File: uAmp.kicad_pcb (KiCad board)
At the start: 2 copper layers, 45 x 24 mm, 18 parts, among them J1 PinHeader_1x07, U1 THAT1512P08-U

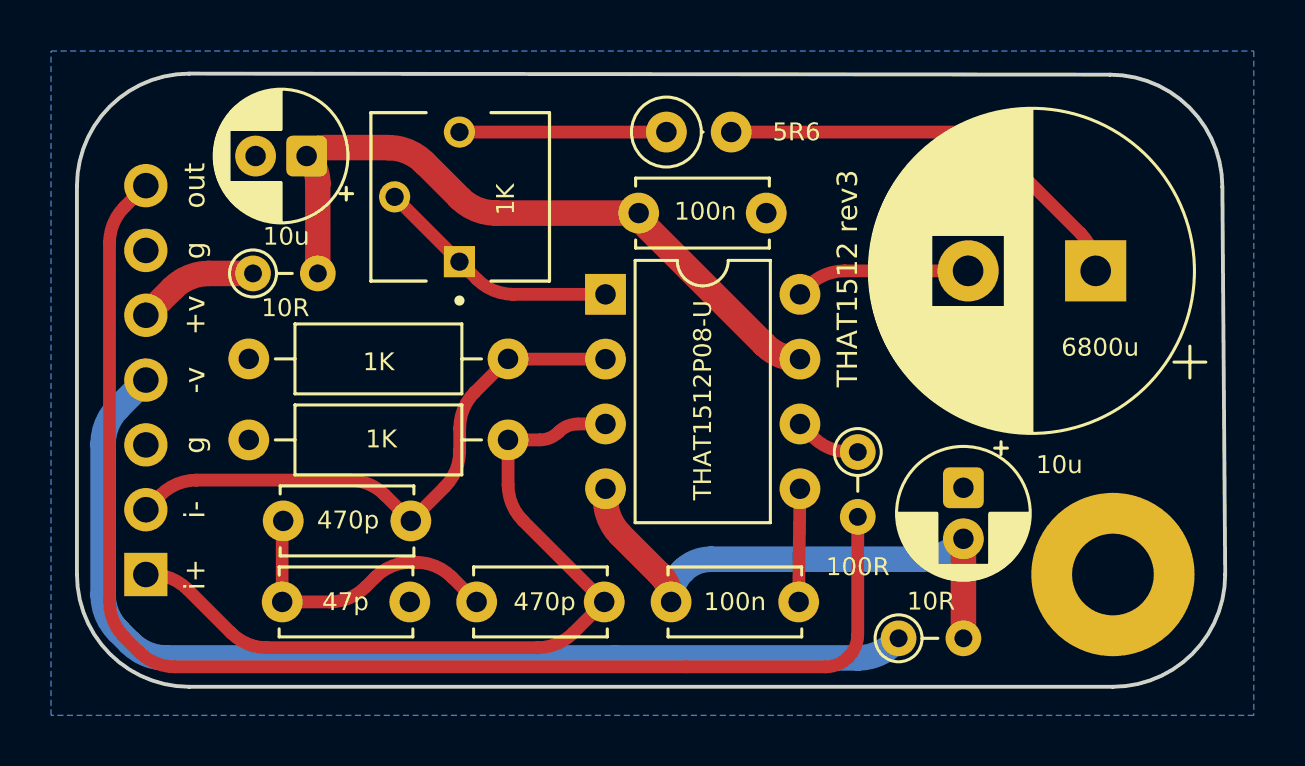
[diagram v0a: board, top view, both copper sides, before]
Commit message: Rename to uAmp; rev3 layout rework, C6 part number, rev2-style render
- Project renamed thatmicpre -> uAmp (files, README title, backups ignore).
- Layout (owner): U1, RV1, C5-C8, R1, R2, R4, R6 moved; GND pour now on
  both layers; header silk relabelled OUT/GND/+15V/-15V/GND/IN-/IN+;
  "uAmp" and "REV.3" added.
- Tidy after the moves: unfillet, collapse drag stubs, redraw seven
  jogged runs (U1 pins 2/3/4/6/7, R4-C7, C6 pad 1) as clean 45-degree
  paths, delete an accidental B.Cu duplicate of the +15V J1-R4 run, J1
  pad 6 solid to the pour, then re-fillet (one corner by RV1 at 0.8 mm
  to keep clearance). Placement, silk and pour untouched by the tidy.
  DRC with schematic parity: 0 errors, 0 unconnected, 0 parity.
- C6 = Nichicon UVZ0J682MHD (6800 uF 6.3 V, 12.5 x 25 mm, 5 mm pitch) in
  schematic, board and BOM; polarized is correct at zero bias, and no
  bipolar 6800 uF fits the footprint.
- README: SSM2019 substitution notes (owner).
- uAmp_rev3_render.png: the rev2 Blender scene (camera, tuned lights,
  world, shadow catcher) with the rev3 board swapped in and per-resistor
  colour bands, composited in Photoshop with the owner's backdrop and
  grade (the PSD is not in the repo). schematic.pdf regenerated.

Co-Authored-By: Claude Opus 5.5 <noreply@anthropic.com>
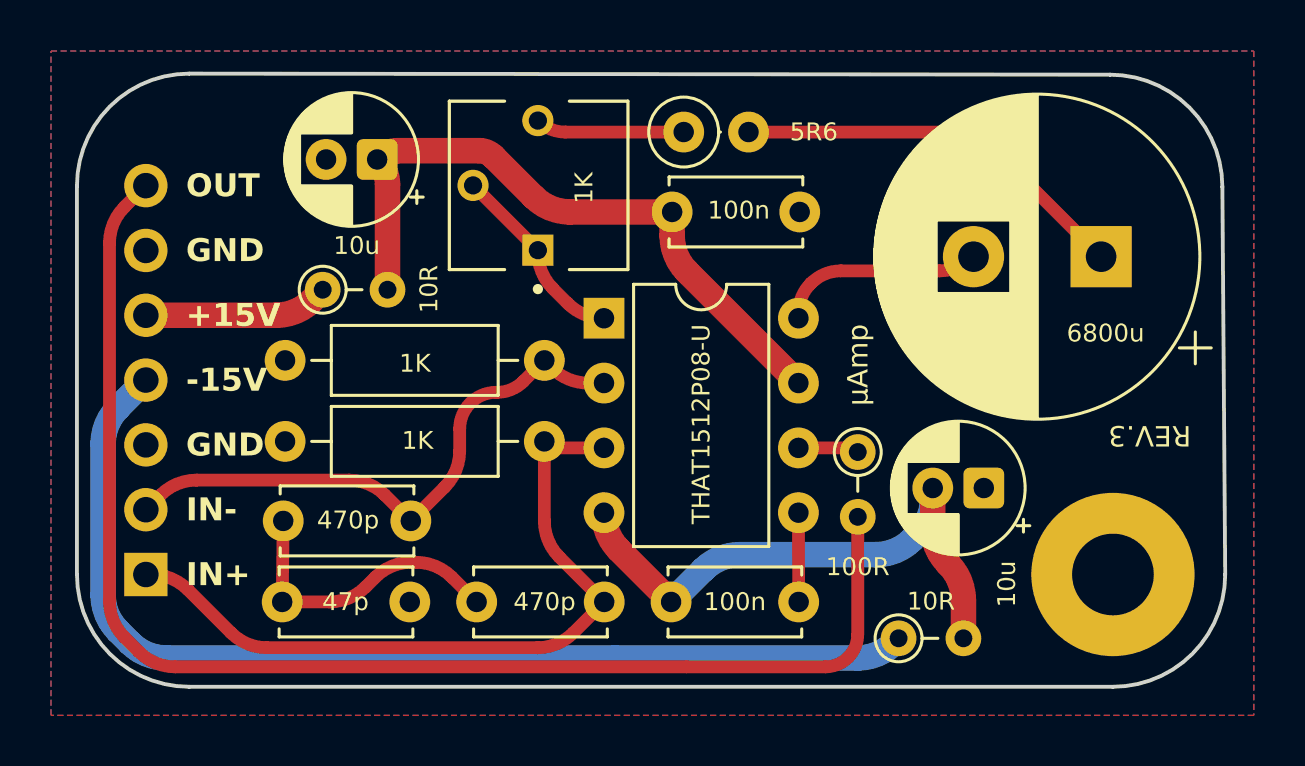
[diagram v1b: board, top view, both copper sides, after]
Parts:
- moved RV1 3.11 mm to (102.5, 57.1)
- moved R4 2.80 mm to (94.0, 61.2)
- moved C7 2.77 mm to (96.2, 56.1)
- moved R2 1.42 mm to (92.6, 67.2)
- moved R1 1.42 mm to (92.6, 64.0)
- moved C5 1.31 mm to (112.7, 58.2)
- moved U1 0.94 mm to (105.1, 62.4)
- moved C8 0.80 mm to (119.9, 69.0), turned to 180 degrees
- moved R6 0.68 mm to (108.2, 55.1)
- moved C6 0.60 mm to (124.5, 59.9)
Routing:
- net +15V: track 4.78 -> 7.25 mm
- net Net-(R6-Pad1): track 8.11 -> 5.83 mm
- net +In: track 31.4 -> 29.2 mm
- net Net-(U1-RG1): track 9.75 -> 7.63 mm
- net /-15V_F: track 21.9 -> 23.2 mm
- net Net-(U1-RG2): track 6.87 -> 8.13 mm
- net Net-(C6-Pad1): track 16.9 -> 15.7 mm
- net /+15V_F: track 27.4 -> 26.4 mm
- net GND: track 4.44 -> 3.50 mm
- added copper zone on F.Cu, net GND
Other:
- board text added: "+15V"
- board text added: "-15V"
- board text added: "GND"
- board text added: "IN+"
- board text added: "IN-"
- board text added: "OUT"
- board text added: "REV.3"
- board text added: "µAmp"
- board text removed: "+v"
- board text removed: "-v"
- board text removed: "THAT1512 rev3"
- board text removed: "g"
- board text removed: "i+"
- board text removed: "i-"
- board text removed: "out"

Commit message: rev3 board as saved 2026-10-04; JLCPCB bare-board package
Board: silk rework (µAmp Mic Pre knockout with a composed µ, SSM2019, 2026,
TRIGLAV MODULAR on the back), the JLCJLCJLCJLC marker removed, zones refilled,
dipped-ceramic 3D models for C1-C5 in 3dmodels/. Render redone.

fab/uAmp_JLCPCB_2026-10-04: gerbers and drill from this save (sha256
7fce3061e375), no BOM or placement file. DRC 0 errors, 0 unconnected.

Co-Authored-By: Claude Fable 5.1 <noreply@anthropic.com>
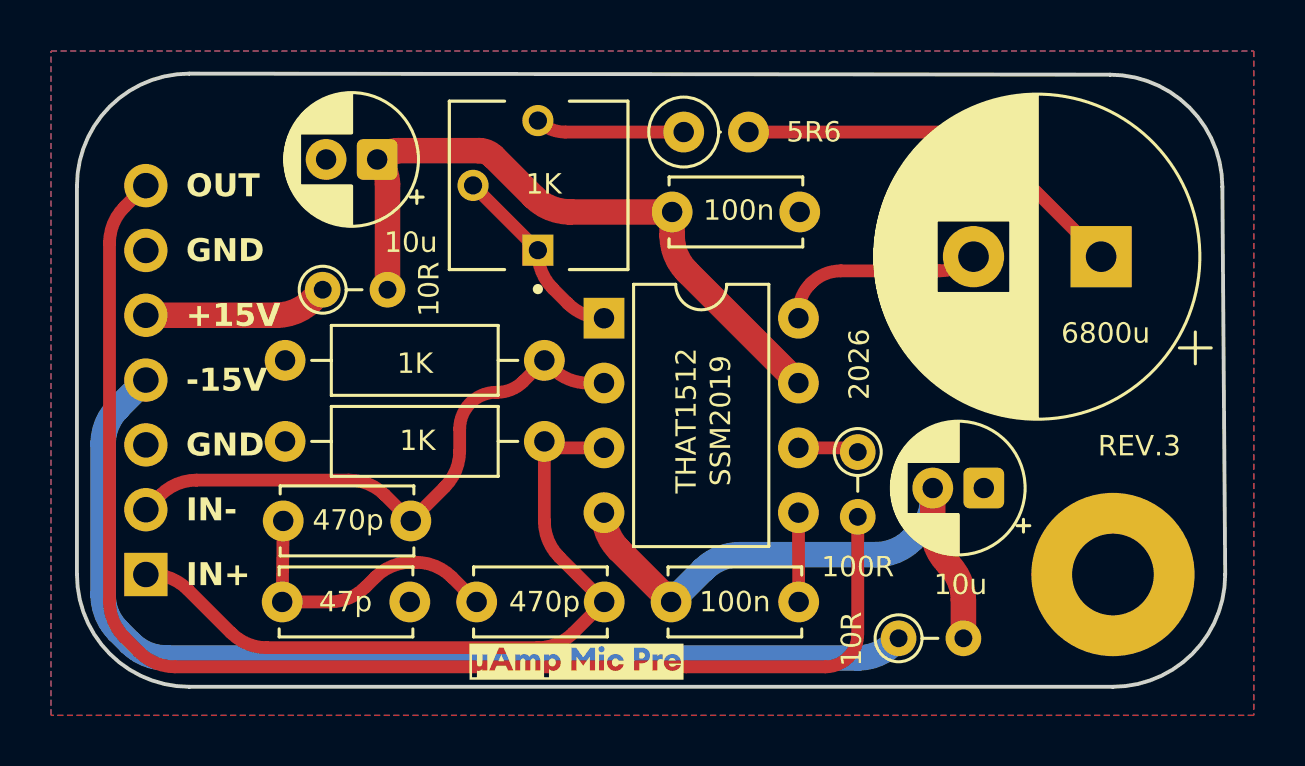
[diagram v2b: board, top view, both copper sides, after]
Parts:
- U1: value THAT1512P08-U -> THAT1512
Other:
- board text added: "2026"
- board text added: "SSM2019"
- board text added: "TRIGLAV MODULAR"
- board text added: "µAmp Mic Pre"
- board text removed: "JLCJLCJLCJLC"
- board text removed: "THAT1512 Mic Pre rev3 2026"
- board text removed: "µAmp"
